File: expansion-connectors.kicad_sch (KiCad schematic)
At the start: 6 parts, among them J10 LSHM-130-01-L-RH-A-S-K-TR

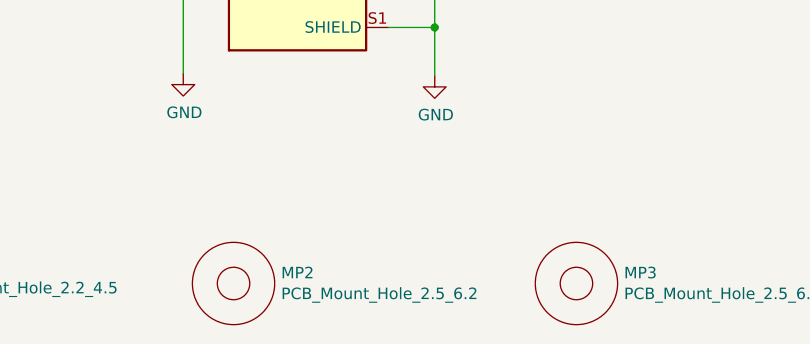
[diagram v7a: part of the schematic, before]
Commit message: Update MP2, MP3 symbol and footprint
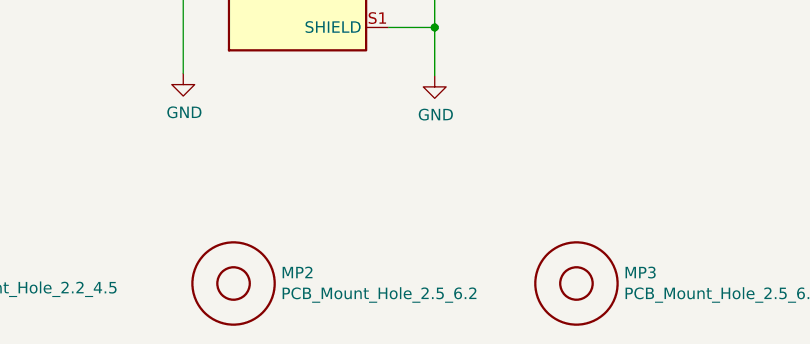
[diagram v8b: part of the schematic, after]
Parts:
- MP2, MP3: footprint scalenode-cm4-baseboard-footprints:Mount-hole-M2.5 -> antmicro-footprints:Mount-hole-M2.5; symbol scalenode-cm4-baseboard:PCB_Mount_Hole_2.5_6.2 -> antmicroMechanicalParts:PCB_Mount_Hole_2.5_6.2; Author (none) -> Antmicro; License (none) -> Apache-2.0; Manufacturer (none) -> None
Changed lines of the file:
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@@
     )
   )
-  (symbol (lib_id "scalenode-cm4-baseboard:PCB_Mount_Hole_2.5_6.2") (at 175.26 196.85 0) (unit 1)
+  (symbol (lib_id "antmicroMechanicalParts:PCB_Mount_Hole_2.5_6.2") (at 175.26 196.85 0) (unit 1)
     (in_bom yes) (on_board yes)
     (property "Reference" "MP2" (id 0) (at 180.5432 195.6816 0)
@@
       (effects (font (size 1.27 1.27)) (justify left))
     )
-    (property "Footprint" "scalenode-cm4-baseboard-footprints:Mount-hole-M2.5" (id 2) (at 195.58 179.07 0)
-      (effects (font (size 1.27 1.27)) hide)
+    (property "Footprint" "antmicro-footprints:Mount-hole-M2.5" (id 2) (at 193.04 204.47 0)
+      (effects (font (size 1.27 1.27) (thickness 0.15)) (justify left bottom) hide)
     )
-    (property "Datasheet" "" (id 3) (at 199.39 176.53 0)
-      (effects (font (size 1.27 1.27)) hide)
+    (property "Datasheet" "" (id 3) (at 193.04 207.01 0)
+      (effects (font (size 1.27 1.27) (thickness 0.15)) (justify left bottom) hide)
+    )
+    (property "Manufacturer" "None" (id 4) (at 193.04 209.55 0)
+      (effects (font (size 1.27 1.27) (thickness 0.15)) (justify left bottom) hide)
+    )
+    (property "Author" "Antmicro" (id 5) (at 193.04 212.09 0)
+      (effects (font (size 1.27 1.27) (thickness 0.15)) (justify left bottom) hide)
+    )
+    (property "License" "Apache-2.0" (id 6) (at 193.04 214.63 0)
+      (effects (font (size 1.27 1.27) (thickness 0.15)) (justify left bottom) hide)
     )
   )
-  (symbol (lib_id "scalenode-cm4-baseboard:PCB_Mount_Hole_2.5_6.2") (at 213.36 196.85 0) (unit 1)
+  (symbol (lib_id "antmicroMechanicalParts:PCB_Mount_Hole_2.5_6.2") (at 213.36 196.85 0) (unit 1)
     (in_bom yes) (on_board yes)
     (property "Reference" "MP3" (id 0) (at 218.6432 195.6816 0)
@@
       (effects (font (size 1.27 1.27)) (justify left))
     )
-    (property "Footprint" "scalenode-cm4-baseboard-footprints:Mount-hole-M2.5" (id 2) (at 233.68 179.07 0)
-      (effects (font (size 1.27 1.27)) hide)
+    (property "Footprint" "antmicro-footprints:Mount-hole-M2.5" (id 2) (at 231.14 204.47 0)
+      (effects (font (size 1.27 1.27) (thickness 0.15)) (justify left bottom) hide)
     )
-    (property "Datasheet" "" (id 3) (at 237.49 176.53 0)
-      (effects (font (size 1.27 1.27)) hide)
+    (property "Datasheet" "" (id 3) (at 231.14 207.01 0)
+      (effects (font (size 1.27 1.27) (thickness 0.15)) (justify left bottom) hide)
+    )
+    (property "Manufacturer" "None" (id 4) (at 231.14 209.55 0)
+      (effects (font (size 1.27 1.27) (thickness 0.15)) (justify left bottom) hide)
+    )
+    (property "Author" "Antmicro" (id 5) (at 231.14 212.09 0)
+      (effects (font (size 1.27 1.27) (thickness 0.15)) (justify left bottom) hide)
+    )
+    (property "License" "Apache-2.0" (id 6) (at 231.14 214.63 0)
+      (effects (font (size 1.27 1.27) (thickness 0.15)) (justify left bottom) hide)
     )
   )
